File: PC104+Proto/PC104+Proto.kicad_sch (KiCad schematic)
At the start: 23 parts, among them J1 Conn_02x32_Odd_Even, J2 Conn_02x20_Odd_Even, J3A1 Conn_02x30_Row_Letter_First, J3C1 Conn_02x30_Row_Letter_First, J4 GROUND

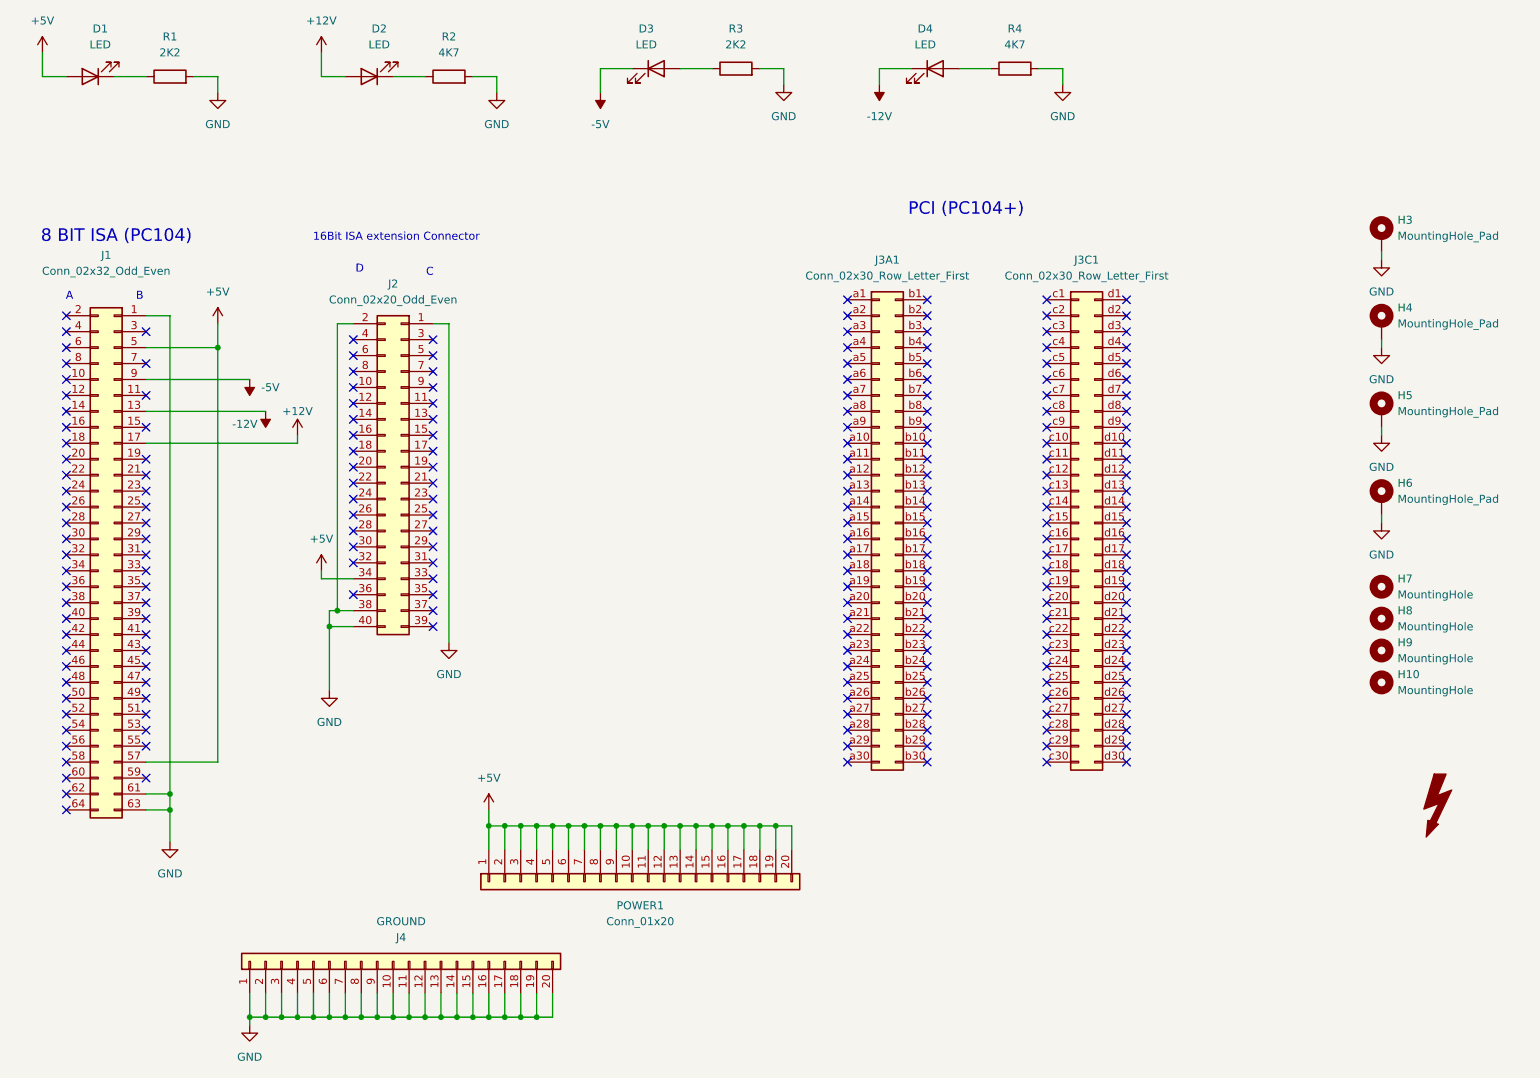
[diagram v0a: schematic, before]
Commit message: Updated .gitignore and added rev1.1 of Protoboard
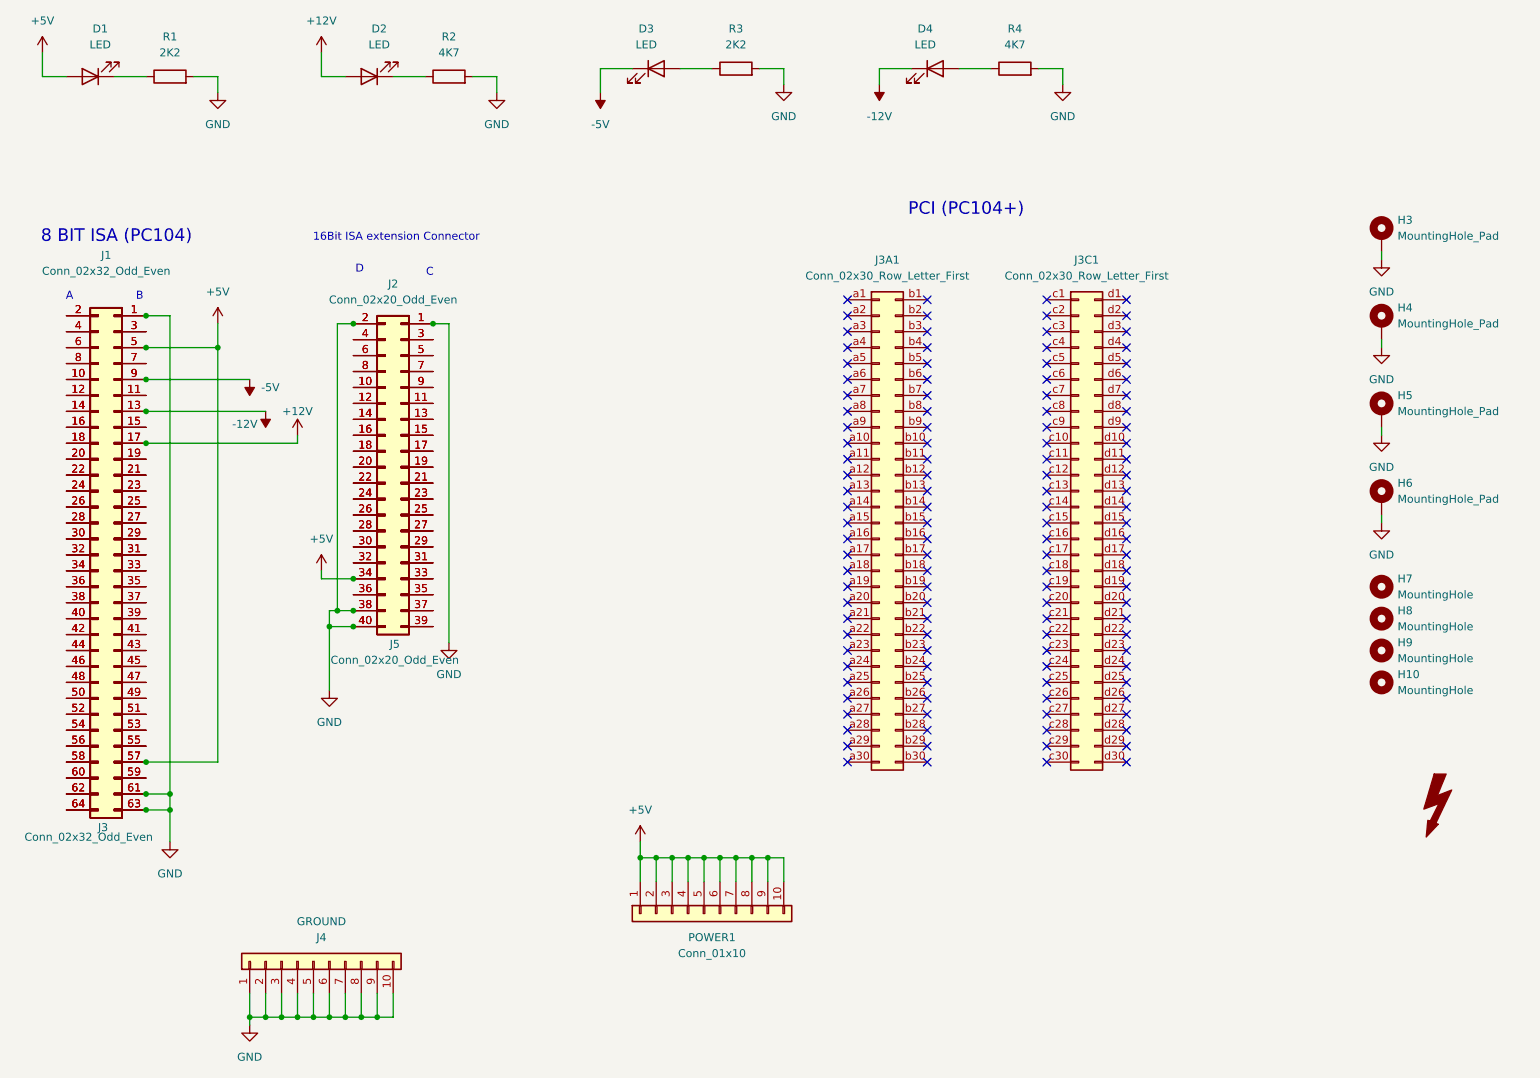
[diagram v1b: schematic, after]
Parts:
- removed J4: GROUND, Connector_PinSocket_2.54mm:PinSocket_1x20_P2.54mm_Vertical, symbol Connector_Generic:Conn_01x20
- removed POWER1: Conn_01x20, Connector_PinSocket_2.54mm:PinSocket_1x20_P2.54mm_Vertical, symbol Connector_Generic:Conn_01x20
- added J3: Conn_02x32_Odd_Even, Connector_PinSocket_2.54mm:PinSocket_2x32_P2.54mm_Vertical, symbol Connector_Generic:Conn_02x32_Odd_Even
- added J4: GROUND, Connector_PinHeader_2.54mm:PinHeader_1x10_P2.54mm_Vertical, symbol Connector_Generic:Conn_01x10
- added J5: Conn_02x20_Odd_Even, Connector_PinSocket_2.54mm:PinSocket_2x20_P2.54mm_Vertical, symbol Connector_Generic:Conn_02x20_Odd_Even
- added POWER1: Conn_01x10, Connector_PinHeader_2.54mm:PinHeader_1x10_P2.54mm_Vertical, symbol Connector_Generic:Conn_01x10
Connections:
- net +12V: now also J3.17 (Pin_17)
- net +5V: now also J3.5 (Pin_5), J3.57 (Pin_57), J5.34 (Pin_34), POWER1.1 (Pin_1), POWER1.10 (Pin_10), POWER1.2 (Pin_2), POWER1.3 (Pin_3), POWER1.4 (Pin_4), POWER1.5 (Pin_5), POWER1.6 (Pin_6), POWER1.7 (Pin_7), POWER1.8 (Pin_8), POWER1.9 (Pin_9)
- net -12V: now also J3.13 (Pin_13)
- net -5V: now also J3.9 (Pin_9)
- net GND: now also J3.1 (Pin_1), J3.61 (Pin_61), J3.63 (Pin_63), J4.1 (Pin_1), J4.10 (Pin_10), J4.2 (Pin_2), J4.3 (Pin_3), J4.4 (Pin_4), J4.5 (Pin_5), J4.6 (Pin_6), J4.7 (Pin_7), J4.8 (Pin_8), J4.9 (Pin_9), J5.1 (Pin_1), J5.2 (Pin_2), J5.38 (Pin_38), J5.40 (Pin_40)
- net at J1.10 (Pin_10): now also J3.10 (Pin_10)
- net at J1.11 (Pin_11): now also J3.11 (Pin_11)
- net at J1.12 (Pin_12): now also J3.12 (Pin_12)
- net at J1.14 (Pin_14): now also J3.14 (Pin_14)
- net at J1.15 (Pin_15): now also J3.15 (Pin_15)
- net at J1.16 (Pin_16): now also J3.16 (Pin_16)
- net at J1.18 (Pin_18): now also J3.18 (Pin_18)
- net at J1.19 (Pin_19): now also J3.19 (Pin_19)
- net at J1.2 (Pin_2): now also J3.2 (Pin_2)
- net at J1.20 (Pin_20): now also J3.20 (Pin_20)
- net at J1.21 (Pin_21): now also J3.21 (Pin_21)
- net at J1.22 (Pin_22): now also J3.22 (Pin_22)
- net at J1.23 (Pin_23): now also J3.23 (Pin_23)
- net at J1.24 (Pin_24): now also J3.24 (Pin_24)
- net at J1.25 (Pin_25): now also J3.25 (Pin_25)
- net at J1.26 (Pin_26): now also J3.26 (Pin_26)
- net at J1.27 (Pin_27): now also J3.27 (Pin_27)
- net at J1.28 (Pin_28): now also J3.28 (Pin_28)
- net at J1.29 (Pin_29): now also J3.29 (Pin_29)
- net at J1.3 (Pin_3): now also J3.3 (Pin_3)
- net at J1.30 (Pin_30): now also J3.30 (Pin_30)
- net at J1.31 (Pin_31): now also J3.31 (Pin_31)
- net at J1.32 (Pin_32): now also J3.32 (Pin_32)
- net at J1.33 (Pin_33): now also J3.33 (Pin_33)
- net at J1.34 (Pin_34): now also J3.34 (Pin_34)
- net at J1.35 (Pin_35): now also J3.35 (Pin_35)
- net at J1.36 (Pin_36): now also J3.36 (Pin_36)
- net at J1.37 (Pin_37): now also J3.37 (Pin_37)
- net at J1.38 (Pin_38): now also J3.38 (Pin_38)
- net at J1.39 (Pin_39): now also J3.39 (Pin_39)
- net at J1.4 (Pin_4): now also J3.4 (Pin_4)
- net at J1.40 (Pin_40): now also J3.40 (Pin_40)
- net at J1.41 (Pin_41): now also J3.41 (Pin_41)
- net at J1.42 (Pin_42): now also J3.42 (Pin_42)
- net at J1.43 (Pin_43): now also J3.43 (Pin_43)
- net at J1.44 (Pin_44): now also J3.44 (Pin_44)
- net at J1.45 (Pin_45): now also J3.45 (Pin_45)
- net at J1.46 (Pin_46): now also J3.46 (Pin_46)
- net at J1.47 (Pin_47): now also J3.47 (Pin_47)
- net at J1.48 (Pin_48): now also J3.48 (Pin_48)
- net at J1.49 (Pin_49): now also J3.49 (Pin_49)
- net at J1.50 (Pin_50): now also J3.50 (Pin_50)
- net at J1.51 (Pin_51): now also J3.51 (Pin_51)
- net at J1.52 (Pin_52): now also J3.52 (Pin_52)
- net at J1.53 (Pin_53): now also J3.53 (Pin_53)
- net at J1.54 (Pin_54): now also J3.54 (Pin_54)
- net at J1.55 (Pin_55): now also J3.55 (Pin_55)
- net at J1.56 (Pin_56): now also J3.56 (Pin_56)
- net at J1.58 (Pin_58): now also J3.58 (Pin_58)
- net at J1.59 (Pin_59): now also J3.59 (Pin_59)
- net at J1.6 (Pin_6): now also J3.6 (Pin_6)
- net at J1.60 (Pin_60): now also J3.60 (Pin_60)
- net at J1.62 (Pin_62): now also J3.62 (Pin_62)
- net at J1.64 (Pin_64): now also J3.64 (Pin_64)
- net at J1.7 (Pin_7): now also J3.7 (Pin_7)
- net at J1.8 (Pin_8): now also J3.8 (Pin_8)
- net at J2.10 (Pin_10): now also J5.10 (Pin_10)
- net at J2.11 (Pin_11): now also J5.11 (Pin_11)
- net at J2.12 (Pin_12): now also J5.12 (Pin_12)
- net at J2.13 (Pin_13): now also J5.13 (Pin_13)
- net at J2.14 (Pin_14): now also J5.14 (Pin_14)
- net at J2.15 (Pin_15): now also J5.15 (Pin_15)
- net at J2.16 (Pin_16): now also J5.16 (Pin_16)
- net at J2.17 (Pin_17): now also J5.17 (Pin_17)
- net at J2.18 (Pin_18): now also J5.18 (Pin_18)
- net at J2.19 (Pin_19): now also J5.19 (Pin_19)
- net at J2.20 (Pin_20): now also J5.20 (Pin_20)
- net at J2.21 (Pin_21): now also J5.21 (Pin_21)
- net at J2.22 (Pin_22): now also J5.22 (Pin_22)
- net at J2.23 (Pin_23): now also J5.23 (Pin_23)
- net at J2.24 (Pin_24): now also J5.24 (Pin_24)
- net at J2.25 (Pin_25): now also J5.25 (Pin_25)
- net at J2.26 (Pin_26): now also J5.26 (Pin_26)
- net at J2.27 (Pin_27): now also J5.27 (Pin_27)
- net at J2.28 (Pin_28): now also J5.28 (Pin_28)
- net at J2.29 (Pin_29): now also J5.29 (Pin_29)
- net at J2.3 (Pin_3): now also J5.3 (Pin_3)
- net at J2.30 (Pin_30): now also J5.30 (Pin_30)
- net at J2.31 (Pin_31): now also J5.31 (Pin_31)
- net at J2.32 (Pin_32): now also J5.32 (Pin_32)
- net at J2.33 (Pin_33): now also J5.33 (Pin_33)
- net at J2.35 (Pin_35): now also J5.35 (Pin_35)
- net at J2.36 (Pin_36): now also J5.36 (Pin_36)
- net at J2.37 (Pin_37): now also J5.37 (Pin_37)
- net at J2.39 (Pin_39): now also J5.39 (Pin_39)
- net at J2.4 (Pin_4): now also J5.4 (Pin_4)
- net at J2.5 (Pin_5): now also J5.5 (Pin_5)
- net at J2.6 (Pin_6): now also J5.6 (Pin_6)
- net at J2.7 (Pin_7): now also J5.7 (Pin_7)
- net at J2.8 (Pin_8): now also J5.8 (Pin_8)
- net at J2.9 (Pin_9): now also J5.9 (Pin_9)
- no-connect marks 211 -> 120
